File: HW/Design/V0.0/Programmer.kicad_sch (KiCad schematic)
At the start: 19 parts, among them J4 SIL04, Q5 SI2302, U5 AVRxxDU28

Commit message: PIC16-DevKit-PCB-877 layout update 4
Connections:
- net +5V: no longer R19.1, R27.1
- new net +VDDTG: R19.1, R27.1
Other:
- moved on the sheet: R19
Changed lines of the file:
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@@
 	(hierarchical_label "TG_PGC"
 		(shape output)
-		(at 79.375 54.61 270)
+		(at 82.55 54.61 270)
 		(fields_autoplaced yes)
 		(effects
@@
 	)
 	(symbol
-		(lib_name "+5V_1")
-		(lib_id "power:+5V")
-		(at 76.2 46.99 0)
+		(lib_id "power:GND")
+		(at 76.2 36.83 0)
+		(mirror y)
 		(unit 1)
 		(exclude_from_sim no)
@@
 		(on_board yes)
 		(dnp no)
-		(property "Reference" "#PWR071"
-			(at 76.2 50.8 0)
+		(property "Reference" "#PWR088"
+			(at 76.2 43.18 0)
 			(effects
 				(font
 					(face "Consolas")
 					(size 1.27 1.27)
-					(thickness 0.254)
 					(bold yes)
 				)
@@
 			)
 		)
-		(property "Value" "+5V"
-			(at 76.2 43.18 0)
+		(property "Value" "GND"
+			(at 76.2 40.64 0)
 			(effects
 				(font
 					(face "Consolas")
 					(size 1.016 1.016)
-					(thickness 0.254)
 				)
 			)
 		)
 		(property "Footprint" ""
-			(at 76.2 46.99 0)
+			(at 76.2 36.83 0)
 			(effects
 				(font
 					(face "Consolas")
 					(size 1.016 1.016)
-					(thickness 0.254)
 				)
 				(hide yes)
@@
 		)
 		(property "Datasheet" ""
-			(at 76.2 46.99 0)
+			(at 76.2 36.83 0)
 			(effects
 				(font
 					(face "Consolas")
 					(size 1.016 1.016)
-					(thickness 0.254)
 				)
 				(hide yes)
 			)
 		)
-		(property "Description" "Power symbol creates a global label with name \"+5V\""
-			(at 76.2 46.99 0)
+		(property "Description" "Power symbol creates a global label with name \"GND\" , ground"
+			(at 76.2 36.83 0)
 			(effects
 				(font
 					(face "Consolas")
 					(size 1.016 1.016)
-					(thickness 0.254)
 				)
 				(hide yes)
@@
 			(project "PIC16DevKit"
 				(path "/17281b91-3f9a-4e36-96b2-66002b412b3a/6fab4358-8edb-4c81-8f5e-6901c5551004"
-					(reference "#PWR071")
+					(reference "#PWR088")
 					(unit 1)
 				)
@@
 	)
 	(symbol
-		(lib_id "power:GND")
-		(at 76.2 36.83 0)
-		(mirror y)
+		(lib_id "power:+3.3V")
+		(at 82.55 46.99 0)
 		(unit 1)
 		(exclude_from_sim no)
@@
 		(on_board yes)
 		(dnp no)
-		(property "Reference" "#PWR088"
-			(at 76.2 43.18 0)
+		(property "Reference" "#PWR020"
+			(at 82.55 50.8 0)
 			(effects
 				(font
@@
 			)
 		)
-		(property "Value" "GND"
-			(at 76.2 40.64 0)
+		(property "Value" "+VDDTG"
+			(at 82.55 43.18 0)
 			(effects
 				(font
@@
 		)
 		(property "Footprint" ""
-			(at 76.2 36.83 0)
+			(at 82.55 46.99 0)
 			(effects
 				(font
@@
 		)
 		(property "Datasheet" ""
-			(at 76.2 36.83 0)
+			(at 82.55 46.99 0)
 			(effects
 				(font
@@
 			)
 		)
-		(property "Description" "Power symbol creates a global label with name \"GND\" , ground"
-			(at 76.2 36.83 0)
+		(property "Description" "Power symbol creates a global label with name \"+3.3V\""
+			(at 82.55 46.99 0)
 			(effects
 				(font
@@
 			(project "PIC16DevKit"
 				(path "/17281b91-3f9a-4e36-96b2-66002b412b3a/6fab4358-8edb-4c81-8f5e-6901c5551004"
-					(reference "#PWR088")
+					(reference "#PWR020")
 					(unit 1)
 				)
@@
 	)
 	(symbol
+		(lib_id "power:+3.3V")
+		(at 76.2 46.99 0)
+		(unit 1)
+		(exclude_from_sim no)
+		(in_bom yes)
+		(on_board yes)
+		(dnp no)
+		(property "Reference" "#PWR071"
+			(at 76.2 50.8 0)
+			(effects
+				(font
+					(face "Consolas")
+					(size 1.27 1.27)
+					(bold yes)
+				)
+				(hide yes)
+			)
+		)
+		(property "Value" "+VDDTG"
+			(at 76.2 43.18 0)
+			(effects
+				(font
+					(face "Consolas")
+					(size 1.016 1.016)
+				)
+			)
+		)
+		(property "Footprint" ""
+			(at 76.2 46.99 0)
+			(effects
+				(font
+					(face "Consolas")
+					(size 1.016 1.016)
+				)
+				(hide yes)
+			)
+		)
+		(property "Datasheet" ""
+			(at 76.2 46.99 0)
+			(effects
+				(font
+					(face "Consolas")
+					(size 1.016 1.016)
+				)
+				(hide yes)
+			)
+		)
+		(property "Description" "Power symbol creates a global label with name \"+3.3V\""
+			(at 76.2 46.99 0)
+			(effects
+				(font
+					(face "Consolas")
+					(size 1.016 1.016)
+				)
+				(hide yes)
+			)
+		)
+		(pin "1"
+		)
+		(instances
+			(project "PIC16DevKit"
+				(path "/17281b91-3f9a-4e36-96b2-66002b412b3a/6fab4358-8edb-4c81-8f5e-6901c5551004"
+					(reference "#PWR071")
+					(unit 1)
+				)
+			)
+		)
+	)
+	(symbol
 		(lib_id "power:GND")
 		(at 59.69 36.83 0)
@@
 	)
 	(symbol
-		(lib_name "+5V_1")
-		(lib_id "power:+5V")
-		(at 79.375 46.99 0)
-		(mirror y)
-		(unit 1)
-		(exclude_from_sim no)
-		(in_bom yes)
-		(on_board yes)
-		(dnp no)
-		(property "Reference" "#PWR073"
-			(at 79.375 50.8 0)
-			(effects
-				(font
-					(face "Consolas")
-					(size 1.27 1.27)
-					(thickness 0.254)
-					(bold yes)
-				)
-				(hide yes)
-			)
-		)
-		(property "Value" "+5V"
-			(at 79.375 43.18 0)
-			(effects
-				(font
-					(face "Consolas")
-					(size 1.016 1.016)
-					(thickness 0.254)
-				)
-			)
-		)
-		(property "Footprint" ""
-			(at 79.375 46.99 0)
-			(effects
-				(font
-					(face "Consolas")
-					(size 1.016 1.016)
-					(thickness 0.254)
-				)
-				(hide yes)
-			)
-		)
-		(property "Datasheet" ""
-			(at 79.375 46.99 0)
-			(effects
-				(font
-					(face "Consolas")
-					(size 1.016 1.016)
-					(thickness 0.254)
-				)
-				(hide yes)
-			)
-		)
-		(property "Description" "Power symbol creates a global label with name \"+5V\""
-			(at 79.375 46.99 0)
-			(effects
-				(font
-					(face "Consolas")
-					(size 1.016 1.016)
-					(thickness 0.254)
-				)
-				(hide yes)
-			)
-		)
-		(pin "1"
-		)
-		(instances
-			(project "PIC16DevKit"
-				(path "/17281b91-3f9a-4e36-96b2-66002b412b3a/6fab4358-8edb-4c81-8f5e-6901c5551004"
-					(reference "#PWR073")
-					(unit 1)
-				)
-			)
-		)
-	)
-	(symbol
 		(lib_id "Triet_KiCAD_Sym:RES")
 		(at 30.48 25.4 0)
@@
 	(symbol
 		(lib_id "Triet_KiCAD_Sym:RES")
-		(at 79.375 50.8 0)
+		(at 82.55 50.8 0)
 		(unit 1)
 		(exclude_from_sim no)
@@
 		(dnp no)
 		(property "Reference" "R19"
-			(at 84.455 49.53 0)
+			(at 87.63 49.53 0)
 			(effects
 				(font
@@
 		)
 		(property "Value" "5.1K, 1%"
-			(at 87.63 52.07 0)
+			(at 90.805 52.07 0)
 			(effects
 				(font
@@
 		)
 		(property "Footprint" "SAMPI:RES0603"
-			(at 79.375 51.054 90)
+			(at 82.55 51.054 90)
 			(effects
 				(font
@@
 		)
 		(property "Datasheet" ""
-			(at 79.375 51.054 90)
+			(at 82.55 51.054 90)
 			(effects
 				(font
@@
 		)
 		(property "Description" "RES 5.1K OHM 1% 1/10W 0603"
-			(at 90.805 50.8 0)
+			(at 93.98 50.8 0)
 			(effects
 				(font
@@
 		)
 		(property "MFT" "Yageo"
-			(at 79.375 50.8 0)
+			(at 82.55 50.8 0)
 			(effects
 				(font
@@
 		)
 		(property "MNP" "RC0603FR-075K1L"
-			(at 79.375 50.8 0)
+			(at 82.55 50.8 0)
 			(effects
 				(font

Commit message: PIC16-DevKit-PCB-877 PCB V0.0
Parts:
- added TP1: PGC/B6, SAMPI:TP1MM, symbol SAMPI:TESTPOINT
- added TP2: PGD/B7, SAMPI:TP1MM, symbol SAMPI:TESTPOINT
- BT1: value MODE -> FNC
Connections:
- net TG_PGC: now also TP1.1
- net TG_PGD: now also TP2.1
- net ~{BT_MODE} renamed ~{BT_FNC}
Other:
- company: (none) -> SAMPI DEVELOPMENT KITS
- title: (none) -> PIC16F877A DEV KIT
- moved on the sheet: R19, R27

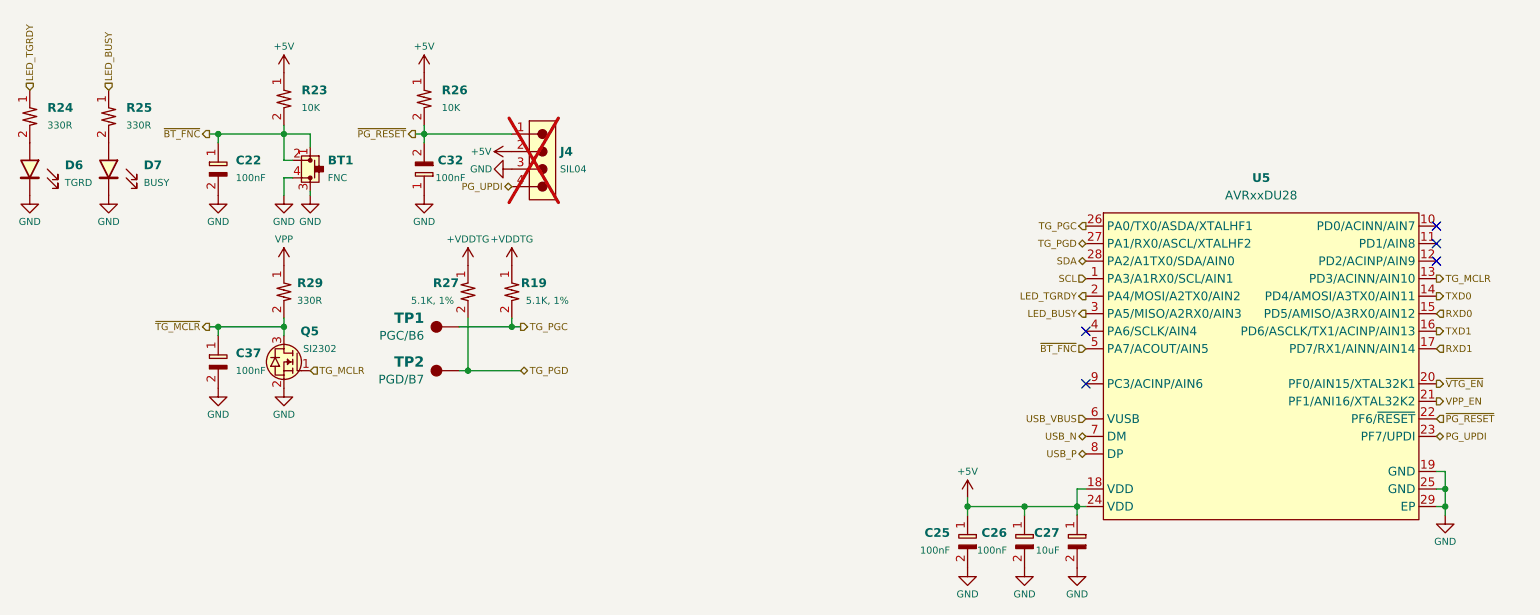
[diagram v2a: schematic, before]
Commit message: PIC16-DevKit-PCB-877 V0.1 - QWIIC ESD protection, disable VPP, detect VBUS, measure VPP, VDDTG
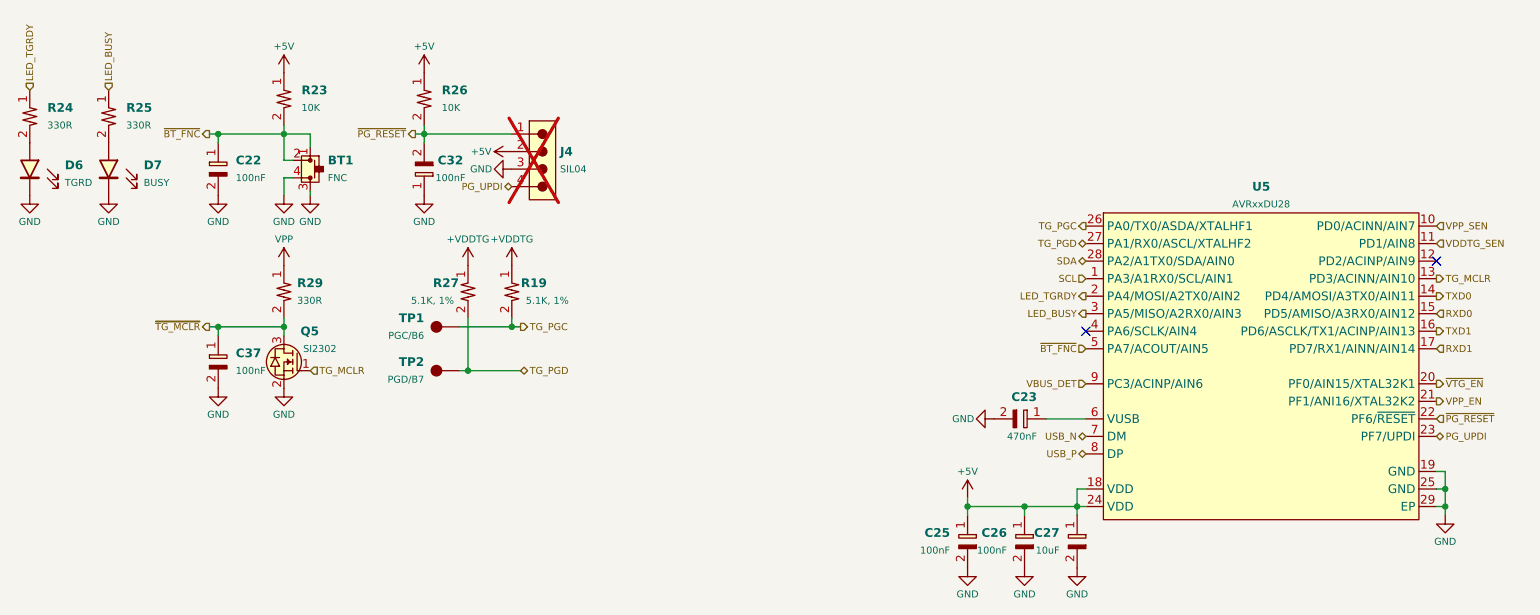
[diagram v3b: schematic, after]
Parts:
- added C23: 470nF, SAMPI:CAP0603, symbol Triet_KiCAD_Sym:CAP_CER
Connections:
- net GND: now also C23.2
- net VPP_SEN: now reaches U5.10 (PD0/ACINN/AIN7)
- net VDDTG_SEN: now reaches U5.11 (PD1/AIN8)
- net VBUS_DET: now reaches U5.9 (PC3/ACINP/AIN6)
- net USB_VBUS: no longer names the net of U5.6 (VUSB)
- net USB_VBUS: now also C23.1
- no-connect marks 5 -> 2
